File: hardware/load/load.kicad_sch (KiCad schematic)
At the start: 9 parts, among them J1 PH2-12-UA, J2 B3B-XH-A, J3 Conn_01x07, J4 Conn_01x07, U1 LP2985-50DBVR

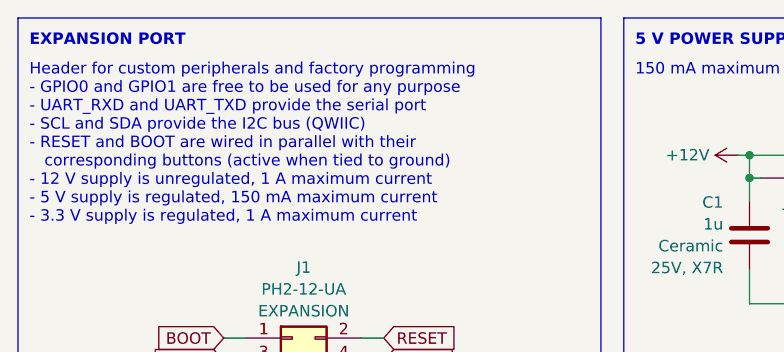
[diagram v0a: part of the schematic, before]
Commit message: Wordsmithing accessories and components.
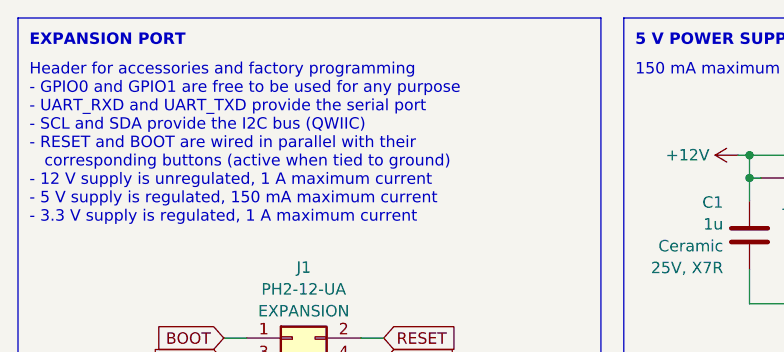
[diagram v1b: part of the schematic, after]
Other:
- note added: "Header for accessories and factory programming - GPIO0 and GPIO1 are free to be used for any purpose - UART_RXD and UART_TXD provide the serial port - SCL and SDA provide the I2C bus (QWIIC) - RESET and BOOT are wired in parallel with their corresponding buttons (active when tied to ground) - 12 V supply is unregulated, 1 A maximum current - 5 V supply is regulated, 150 mA maximum current - 3.3 V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"
- note removed: "Header for custom peripherals and factory programming - GPIO0 and GPIO1 are free to be used for any purpose - UART_RXD and UART_TXD provide the serial port - SCL and SDA provide the I2C bus (QWIIC) - RESET and BOOT are wired in parallel with their corresponding buttons (active when tied to ground) - 12 V supply is unregulated, 1 A maximum current - 5 V supply is regulated, 150 mA maximum current 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"
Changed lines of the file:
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@@
 		)
 	)
-	(text "Header for custom peripherals and factory programming\n- GPIO0 and GPIO1 are free to be used for any purpose\n- UART_RXD and UART_TXD provide the serial port\n- SCL and SDA provide the I2C bus (QWIIC)\n- RESET and BOOT are wired in parallel with their\n   corresponding buttons (active when tied to ground)\n- 12 V supply is unregulated, 1 A maximum current\n- 5 V supply is regulated, 150 mA maximum current\n- 3.3 V supply is regulated, 1 A maximum current"
+	(text "Header for accessories and factory programming\n- GPIO0 and GPIO1 are free to be used for any purpose\n- UART_RXD and UART_TXD provide the serial port\n- SCL and SDA provide the I2C bus (QWIIC)\n- RESET and BOOT are wired in parallel with their\n   corresponding buttons (active when tied to ground)\n- 12 V supply is unregulated, 1 A maximum current\n- 5 V supply is regulated, 150 mA maximum current\n- 3.3 V supply is regulated, 1 A maximum current"
 		(exclude_from_sim no)
 		(at 73.66 58.42 0)

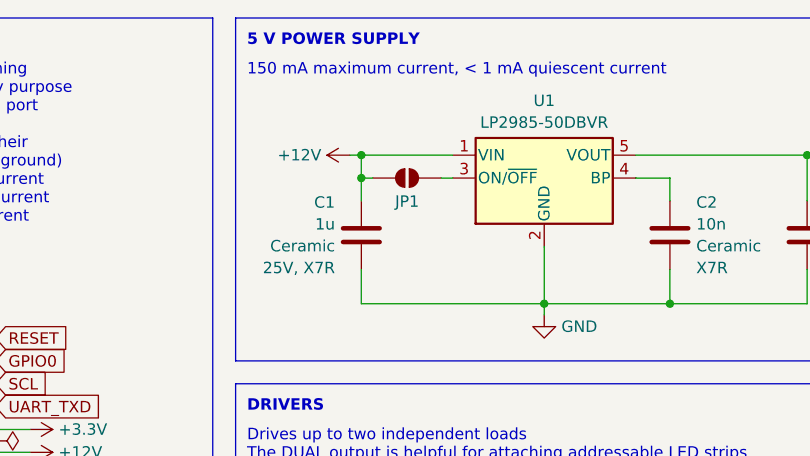
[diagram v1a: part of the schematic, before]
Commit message: Abandon load accessory design, update errata.
Decided to abandon this design because it is overly complex and
doesn't work with addressable LEDs as intended.  It would be better
to design simpler boards for each use-case instead of having lots
of jumpers.
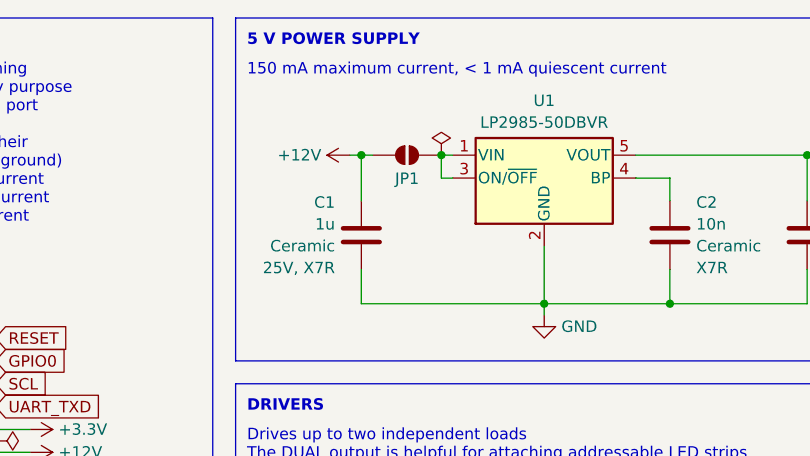
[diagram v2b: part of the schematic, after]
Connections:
- net +12V: no longer U1.1 (VIN)
- net at JP1.2 (B), U1.3 (ON/~{OFF}): now also U1.1 (VIN)
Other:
- moved on the sheet: JP1
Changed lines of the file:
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@@
 		(title "Minuet Lighting and Load Accessory")
 		(date "2025-02")
-		(rev "2.0")
+		(rev "2.1")
 	)
 	(junction
@@
 	)
 	(junction
-		(at 153.67 71.12)
+		(at 111.76 99.06)
 		(diameter 0)
 		(color 0 0 0 0)
 	)
 	(junction
-		(at 111.76 99.06)
+		(at 153.67 68.58)
 		(diameter 0)
 		(color 0 0 0 0)
@@
 	)
 	(junction
-		(at 153.67 68.58)
+		(at 162.56 68.58)
 		(diameter 0)
 		(color 0 0 0 0)
@@
 	(wire
 		(pts
-			(xy 153.67 68.58) (xy 153.67 71.12)
+			(xy 153.67 68.58) (xy 153.67 73.66)
 		)
 		(stroke
@@
 	(wire
 		(pts
-			(xy 153.67 68.58) (xy 163.83 68.58)
-		)
-		(stroke
-			(width 0)
-			(type default)
-		)
-	)
-	(wire
-		(pts
 			(xy 187.96 85.09) (xy 203.2 85.09)
 		)
@@
 	(wire
 		(pts
-			(xy 92.71 120.65) (xy 95.25 120.65)
+			(xy 162.56 68.58) (xy 163.83 68.58)
 		)
 		(stroke
@@
 	(wire
 		(pts
-			(xy 153.67 71.12) (xy 154.94 71.12)
+			(xy 92.71 120.65) (xy 95.25 120.65)
 		)
 		(stroke
@@
 	(wire
 		(pts
-			(xy 180.34 116.84) (xy 180.34 123.19)
+			(xy 153.67 68.58) (xy 154.94 68.58)
 		)
 		(stroke
@@
 	(wire
 		(pts
-			(xy 153.67 71.12) (xy 153.67 73.66)
+			(xy 180.34 116.84) (xy 180.34 123.19)
 		)
 		(stroke
@@
 	(wire
 		(pts
+			(xy 162.56 71.12) (xy 163.83 71.12)
+		)
+		(stroke
+			(width 0)
+			(type default)
+		)
+	)
+	(wire
+		(pts
 			(xy 113.03 96.52) (xy 110.49 96.52)
 		)
@@
 	(wire
 		(pts
-			(xy 97.79 101.6) (xy 96.52 101.6)
+			(xy 162.56 68.58) (xy 162.56 71.12)
 		)
 		(stroke
@@
 	(wire
 		(pts
-			(xy 153.67 81.28) (xy 153.67 85.09)
+			(xy 97.79 101.6) (xy 96.52 101.6)
 		)
 		(stroke
@@
 	(wire
 		(pts
-			(xy 163.83 71.12) (xy 162.56 71.12)
+			(xy 153.67 81.28) (xy 153.67 85.09)
 		)
 		(stroke
@@
 		(dnp no)
 		(fields_autoplaced yes)
-		(property "Reference" "#FLG01"
+		(property "Reference" "#FLG02"
 			(at 114.935 100.33 0)
 			(effects
@@
 			(project "load"
 				(path "/a369f822-a924-4186-8e20-d08fd579731a"
-					(reference "#FLG01")
+					(reference "#FLG02")
 					(unit 1)
 				)
@@
 	)
 	(symbol
+		(lib_id "power:PWR_FLAG")
+		(at 162.56 68.58 0)
+		(unit 1)
+		(exclude_from_sim no)
+		(in_bom yes)
+		(on_board yes)
+		(dnp no)
+		(fields_autoplaced yes)
+		(property "Reference" "#FLG01"
+			(at 162.56 66.675 0)
+			(effects
+				(font
+					(size 1.27 1.27)
+				)
+				(hide yes)
+			)
+		)
+		(property "Value" "PWR_FLAG"
+			(at 162.56 64.4469 0)
+			(effects
+				(font
+					(size 1.27 1.27)
+				)
+				(hide yes)
+			)
+		)
+		(property "Footprint" ""
+			(at 162.56 68.58 0)
+			(effects
+				(font
+					(size 1.27 1.27)
+				)
+				(hide yes)
+			)
+		)
+		(property "Datasheet" "~"
+			(at 162.56 68.58 0)
+			(effects
+				(font
+					(size 1.27 1.27)
+				)
+				(hide yes)
+			)
+		)
+		(property "Description" "Special symbol for telling ERC where power comes from"
+			(at 162.56 68.58 0)
+			(effects
+				(font
+					(size 1.27 1.27)
+				)
+				(hide yes)
+			)
+		)
+		(pin "1"
+		)
+		(instances
+			(project "load"
+				(path "/a369f822-a924-4186-8e20-d08fd579731a"
+					(reference "#FLG01")
+					(unit 1)
+				)
+			)
+		)
+	)
+	(symbol
 		(lib_id "power:+12V")
 		(at 116.84 101.6 270)
@@
 		(dnp no)
 		(fields_autoplaced yes)
-		(property "Reference" "#FLG03"
+		(property "Reference" "#FLG04"
 			(at 111.76 103.505 0)
 			(effects
@@
 			(project "load"
 				(path "/a369f822-a924-4186-8e20-d08fd579731a"
-					(reference "#FLG03")
+					(reference "#FLG04")
 					(unit 1)
 				)
@@
 	(symbol
 		(lib_id "Jumper:SolderJumper_2_Open")
-		(at 158.75 71.12 0)
+		(at 158.75 68.58 0)
 		(unit 1)
 		(exclude_from_sim yes)
@@
 		(dnp no)
 		(property "Reference" "JP1"
-			(at 158.75 73.7291 0)
+			(at 158.75 71.1891 0)
 			(effects
 				(font
@@
 		)
 		(property "Value" "SolderJumper_2_Open"
-			(at 157.5379 72.771 90)
+			(at 157.5379 70.231 90)
 			(effects
 				(font
@@
 		)
 		(property "Footprint" "Jumper:SolderJumper-2_P1.3mm_Open_TrianglePad1.0x1.5mm"
-			(at 158.75 71.12 0)
+			(at 158.75 68.58 0)
 			(effects
 				(font
@@
 		)
 		(property "Datasheet" "~"
-			(at 158.75 71.12 0)
+			(at 158.75 68.58 0)
 			(effects
 				(font
@@
 		)
 		(property "Description" "Solder Jumper, 2-pole, open"
-			(at 158.75 71.12 0)
+			(at 158.75 68.58 0)
 			(effects
 				(font
@@
 		(dnp no)
 		(fields_autoplaced yes)
-		(property "Reference" "#FLG02"
+		(property "Reference" "#FLG03"
 			(at 96.52 103.505 0)
 			(effects
@@
 			(project ""
 				(path "/a369f822-a924-4186-8e20-d08fd579731a"
-					(reference "#FLG02")
+					(reference "#FLG03")
 					(unit 1)
 				)
